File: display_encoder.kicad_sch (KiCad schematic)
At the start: 9 parts

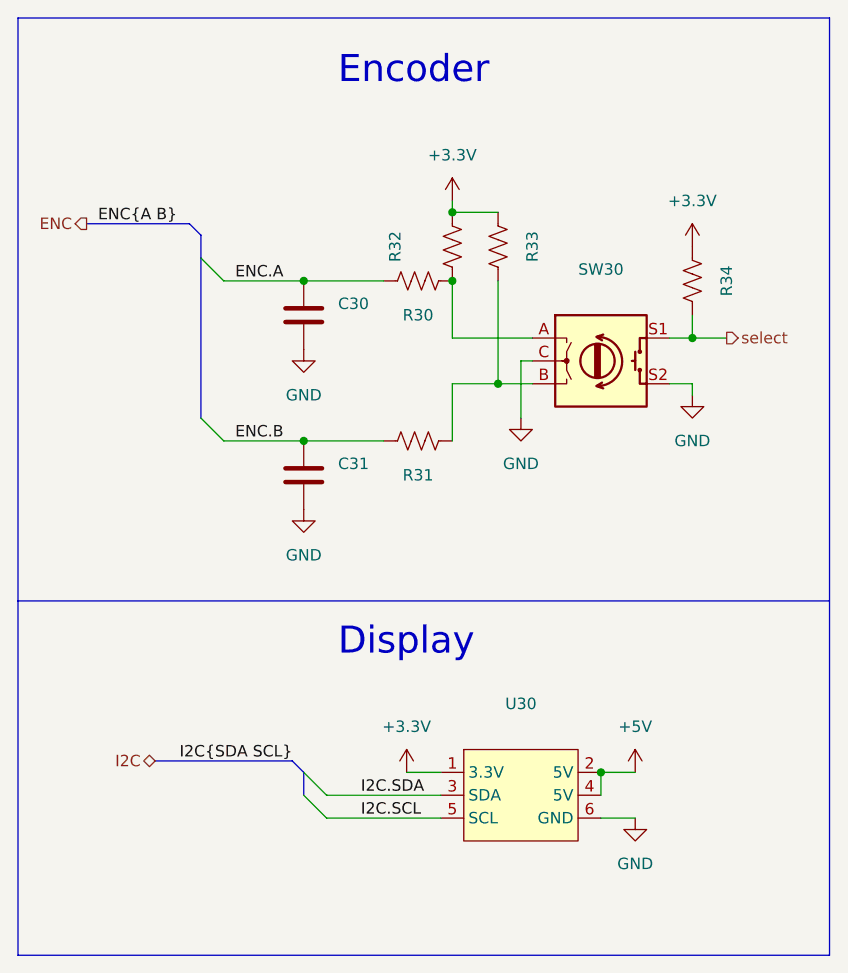
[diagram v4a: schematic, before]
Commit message: Add heatsink, among other things
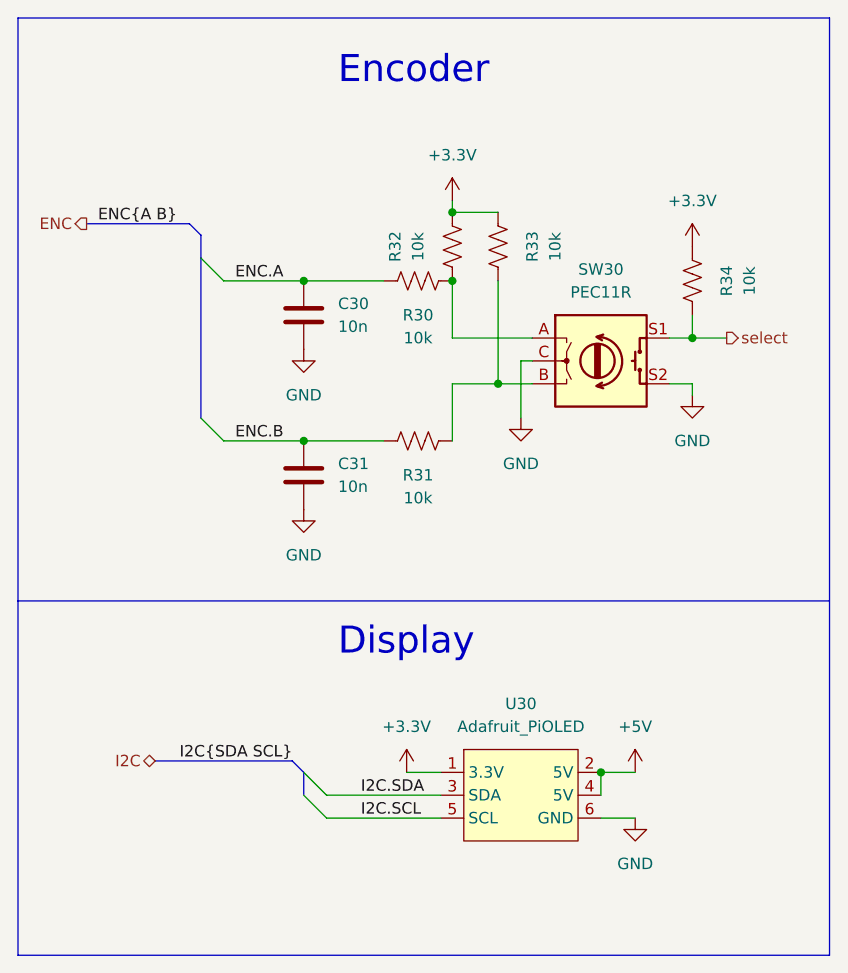
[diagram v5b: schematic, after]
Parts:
- C30, C31: value (none) -> 10n; footprint (none) -> Capacitor_SMD:C_0805_2012Metric
- R30, R31, R32, R33, R34: value (none) -> 10k; footprint (none) -> Resistor_SMD:R_0805_2012Metric
- SW30: value (none) -> PEC11R; footprint (none) -> Rotary_Encoder:RotaryEncoder_Alps_EC12E-Switch_Vertical_H20mm
- U30: value (none) -> Adafruit_PiOLED; footprint (none) -> 0_Display:PiOLED
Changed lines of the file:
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@@
     (in_bom yes) (on_board yes)
     (property "Reference" "R30" (id 0) (at 149.86 73.66 90))
-    (property "Value" "" (id 1) (at 149.86 76.2 90))
-    (property "Footprint" "" (id 2) (at 150.114 68.834 90)
+    (property "Value" "10k" (id 1) (at 149.86 76.2 90))
+    (property "Footprint" "Resistor_SMD:R_0805_2012Metric" (id 2) (at 150.114 68.834 90)
       (effects (font (size 1.27 1.27)) hide)
     )
@@
     (in_bom yes) (on_board yes) (fields_autoplaced)
     (property "Reference" "U30" (id 0) (at 161.29 116.84 0))
-    (property "Value" "" (id 1) (at 161.29 119.38 0))
-    (property "Footprint" "" (id 2) (at 162.56 121.92 0)
+    (property "Value" "Adafruit_PiOLED" (id 1) (at 161.29 119.38 0))
+    (property "Footprint" "0_Display:PiOLED" (id 2) (at 162.56 121.92 0)
       (effects (font (size 1.27 1.27)) hide)
     )
@@
       (effects (font (size 1.27 1.27)) (justify right))
     )
-    (property "Value" "" (id 1) (at 140.97 74.9299 0)
-      (effects (font (size 1.27 1.27)) (justify right))
-    )
-    (property "Footprint" "" (id 2) (at 136.1948 69.85 0)
+    (property "Value" "10n" (id 1) (at 140.97 74.9299 0)
+      (effects (font (size 1.27 1.27)) (justify right))
+    )
+    (property "Footprint" "Capacitor_SMD:C_0805_2012Metric" (id 2) (at 136.1948 69.85 0)
       (effects (font (size 1.27 1.27)) hide)
     )
@@
     (in_bom yes) (on_board yes)
     (property "Reference" "SW30" (id 0) (at 170.18 68.58 0))
-    (property "Value" "" (id 1) (at 170.18 71.12 0))
-    (property "Footprint" "" (id 2) (at 166.37 74.676 0)
+    (property "Value" "PEC11R" (id 1) (at 170.18 71.12 0))
+    (property "Footprint" "Rotary_Encoder:RotaryEncoder_Alps_EC12E-Switch_Vertical_H20mm" (id 2) (at 166.37 74.676 0)
       (effects (font (size 1.27 1.27)) hide)
     )
@@
       (effects (font (size 1.27 1.27)) (justify right))
     )
-    (property "Value" "" (id 1) (at 140.97 92.7099 0)
-      (effects (font (size 1.27 1.27)) (justify right))
-    )
-    (property "Footprint" "" (id 2) (at 136.1948 87.63 0)
+    (property "Value" "10n" (id 1) (at 140.97 92.7099 0)
+      (effects (font (size 1.27 1.27)) (justify right))
+    )
+    (property "Footprint" "Capacitor_SMD:C_0805_2012Metric" (id 2) (at 136.1948 87.63 0)
       (effects (font (size 1.27 1.27)) hide)
     )
@@
     (in_bom yes) (on_board yes)
     (property "Reference" "R32" (id 0) (at 147.32 66.04 90))
-    (property "Value" "" (id 1) (at 149.86 66.04 90))
-    (property "Footprint" "" (id 2) (at 154.686 66.294 90)
+    (property "Value" "10k" (id 1) (at 149.86 66.04 90))
+    (property "Footprint" "Resistor_SMD:R_0805_2012Metric" (id 2) (at 154.686 66.294 90)
       (effects (font (size 1.27 1.27)) hide)
     )
@@
     (in_bom yes) (on_board yes)
     (property "Reference" "R34" (id 0) (at 184.15 69.85 90))
-    (property "Value" "" (id 1) (at 186.69 69.85 90))
-    (property "Footprint" "" (id 2) (at 179.324 69.596 90)
+    (property "Value" "10k" (id 1) (at 186.69 69.85 90))
+    (property "Footprint" "Resistor_SMD:R_0805_2012Metric" (id 2) (at 179.324 69.596 90)
       (effects (font (size 1.27 1.27)) hide)
     )
@@
     (in_bom yes) (on_board yes)
     (property "Reference" "R31" (id 0) (at 149.86 91.44 90))
-    (property "Value" "" (id 1) (at 149.86 93.98 90))
-    (property "Footprint" "" (id 2) (at 150.114 86.614 90)
+    (property "Value" "10k" (id 1) (at 149.86 93.98 90))
+    (property "Footprint" "Resistor_SMD:R_0805_2012Metric" (id 2) (at 150.114 86.614 90)
       (effects (font (size 1.27 1.27)) hide)
     )
@@
     (in_bom yes) (on_board yes)
     (property "Reference" "R33" (id 0) (at 162.56 66.04 90))
-    (property "Value" "" (id 1) (at 165.1 66.04 90))
-    (property "Footprint" "" (id 2) (at 157.734 65.786 90)
-      (effects (font (size 1.27 1.27)) hide)
-    )
+    (property "Value" "10k" (id 1) (at 165.1 66.04 90))
+    (property "Footprint" "Resistor_SMD:R_0805_2012Metric" (id 2) (at 157.734 65.786 90)
+      (effects (font (size 1.27 1.27)) hide)
+    )

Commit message: WIP routing
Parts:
- C601: renamed from C30; value 10n -> (none); footprint Capacitor_SMD:C_0805_2012Metric -> (none)
- C602: renamed from C31; value 10n -> (none); footprint Capacitor_SMD:C_0805_2012Metric -> (none)
- R601: renamed from R30; value 10k -> (none); footprint Resistor_SMD:R_0805_2012Metric -> (none)
- R602: renamed from R31; value 10k -> (none); footprint Resistor_SMD:R_0805_2012Metric -> (none)
- R603: renamed from R32; value 10k -> (none); footprint Resistor_SMD:R_0805_2012Metric -> (none)
- R604: renamed from R33; value 10k -> (none); footprint Resistor_SMD:R_0805_2012Metric -> (none)
- R605: renamed from R34; value 10k -> (none); footprint Resistor_SMD:R_0805_2012Metric -> (none)
- SW601: renamed from SW30; value PEC11R -> (none); footprint Rotary_Encoder:RotaryEncoder_Alps_EC12E-Switch_Vertical_H20mm -> (none)
- U601: renamed from U30; value Adafruit_PiOLED -> (none); footprint 0_Display:PiOLED -> (none)
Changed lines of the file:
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@@
   (symbol (lib_id "power:GND") (at 137.16 77.47 0) (unit 1)
     (in_bom yes) (on_board yes) (fields_autoplaced)
-    (property "Reference" "#PWR0118" (id 0) (at 137.16 83.82 0)
+    (property "Reference" "#PWR0601" (id 0) (at 137.16 83.82 0)
       (effects (font (size 1.27 1.27)) hide)
     )
@@
   (symbol (lib_id "power:+3.3V") (at 180.34 66.04 0) (unit 1)
     (in_bom yes) (on_board yes) (fields_autoplaced)
-    (property "Reference" "#PWR0120" (id 0) (at 180.34 69.85 0)
+    (property "Reference" "#PWR0608" (id 0) (at 180.34 69.85 0)
       (effects (font (size 1.27 1.27)) hide)
     )
@@
   (symbol (lib_id "Device:R_US") (at 149.86 69.85 90) (unit 1)
     (in_bom yes) (on_board yes)
-    (property "Reference" "R30" (id 0) (at 149.86 73.66 90))
-    (property "Value" "10k" (id 1) (at 149.86 76.2 90))
-    (property "Footprint" "Resistor_SMD:R_0805_2012Metric" (id 2) (at 150.114 68.834 90)
+    (property "Reference" "R601" (id 0) (at 149.86 73.66 90))
+    (property "Value" "" (id 1) (at 149.86 76.2 90))
+    (property "Footprint" "" (id 2) (at 150.114 68.834 90)
       (effects (font (size 1.27 1.27)) hide)
     )
@@
   (symbol (lib_id "0_Display_Graphic:Adafruit_PiOLED") (at 161.29 127 0) (unit 1)
     (in_bom yes) (on_board yes) (fields_autoplaced)
-    (property "Reference" "U30" (id 0) (at 161.29 116.84 0))
-    (property "Value" "Adafruit_PiOLED" (id 1) (at 161.29 119.38 0))
-    (property "Footprint" "0_Display:PiOLED" (id 2) (at 162.56 121.92 0)
+    (property "Reference" "U601" (id 0) (at 161.29 116.84 0))
+    (property "Value" "" (id 1) (at 161.29 119.38 0))
+    (property "Footprint" "" (id 2) (at 162.56 121.92 0)
       (effects (font (size 1.27 1.27)) hide)
     )
@@
   (symbol (lib_id "power:GND") (at 173.99 129.54 0) (unit 1)
     (in_bom yes) (on_board yes) (fields_autoplaced)
-    (property "Reference" "#PWR0106" (id 0) (at 173.99 135.89 0)
+    (property "Reference" "#PWR0607" (id 0) (at 173.99 135.89 0)
       (effects (font (size 1.27 1.27)) hide)
     )
@@
   (symbol (lib_id "power:GND") (at 180.34 82.55 0) (unit 1)
     (in_bom yes) (on_board yes) (fields_autoplaced)
-    (property "Reference" "#PWR0119" (id 0) (at 180.34 88.9 0)
+    (property "Reference" "#PWR0609" (id 0) (at 180.34 88.9 0)
       (effects (font (size 1.27 1.27)) hide)
     )
@@
   (symbol (lib_id "power:GND") (at 161.29 85.09 0) (unit 1)
     (in_bom yes) (on_board yes) (fields_autoplaced)
-    (property "Reference" "#PWR0116" (id 0) (at 161.29 91.44 0)
+    (property "Reference" "#PWR0605" (id 0) (at 161.29 91.44 0)
       (effects (font (size 1.27 1.27)) hide)
     )
@@
   (symbol (lib_id "power:GND") (at 137.16 95.25 0) (unit 1)
     (in_bom yes) (on_board yes) (fields_autoplaced)
-    (property "Reference" "#PWR0117" (id 0) (at 137.16 101.6 0)
+    (property "Reference" "#PWR0602" (id 0) (at 137.16 101.6 0)
       (effects (font (size 1.27 1.27)) hide)
     )
@@
   (symbol (lib_id "Device:C") (at 137.16 73.66 180) (unit 1)
     (in_bom yes) (on_board yes) (fields_autoplaced)
-    (property "Reference" "C30" (id 0) (at 140.97 72.3899 0)
-      (effects (font (size 1.27 1.27)) (justify right))
-    )
-    (property "Value" "10n" (id 1) (at 140.97 74.9299 0)
-      (effects (font (size 1.27 1.27)) (justify right))
-    )
-    (property "Footprint" "Capacitor_SMD:C_0805_2012Metric" (id 2) (at 136.1948 69.85 0)
+    (property "Reference" "C601" (id 0) (at 140.97 72.3899 0)
+      (effects (font (size 1.27 1.27)) (justify right))
+    )
+    (property "Value" "" (id 1) (at 140.97 74.9299 0)
+      (effects (font (size 1.27 1.27)) (justify right))
+    )
+    (property "Footprint" "" (id 2) (at 136.1948 69.85 0)
       (effects (font (size 1.27 1.27)) hide)
     )
@@
   (symbol (lib_id "Device:RotaryEncoder_Switch") (at 170.18 78.74 0) (unit 1)
     (in_bom yes) (on_board yes)
-    (property "Reference" "SW30" (id 0) (at 170.18 68.58 0))
-    (property "Value" "PEC11R" (id 1) (at 170.18 71.12 0))
-    (property "Footprint" "Rotary_Encoder:RotaryEncoder_Alps_EC12E-Switch_Vertical_H20mm" (id 2) (at 166.37 74.676 0)
+    (property "Reference" "SW601" (id 0) (at 170.18 68.58 0))
+    (property "Value" "" (id 1) (at 170.18 71.12 0))
+    (property "Footprint" "" (id 2) (at 166.37 74.676 0)
       (effects (font (size 1.27 1.27)) hide)
     )
@@
   (symbol (lib_id "Device:C") (at 137.16 91.44 180) (unit 1)
     (in_bom yes) (on_board yes) (fields_autoplaced)
-    (property "Reference" "C31" (id 0) (at 140.97 90.1699 0)
-      (effects (font (size 1.27 1.27)) (justify right))
-    )
-    (property "Value" "10n" (id 1) (at 140.97 92.7099 0)
-      (effects (font (size 1.27 1.27)) (justify right))
-    )
-    (property "Footprint" "Capacitor_SMD:C_0805_2012Metric" (id 2) (at 136.1948 87.63 0)
+    (property "Reference" "C602" (id 0) (at 140.97 90.1699 0)
+      (effects (font (size 1.27 1.27)) (justify right))
+    )
+    (property "Value" "" (id 1) (at 140.97 92.7099 0)
+      (effects (font (size 1.27 1.27)) (justify right))
+    )
+    (property "Footprint" "" (id 2) (at 136.1948 87.63 0)
       (effects (font (size 1.27 1.27)) hide)
     )
@@
   (symbol (lib_id "power:+3.3V") (at 148.59 124.46 0) (unit 1)
     (in_bom yes) (on_board yes) (fields_autoplaced)
-    (property "Reference" "#PWR0104" (id 0) (at 148.59 128.27 0)
+    (property "Reference" "#PWR0603" (id 0) (at 148.59 128.27 0)
       (effects (font (size 1.27 1.27)) hide)
     )
@@
   (symbol (lib_id "Device:R_US") (at 153.67 66.04 0) (unit 1)
     (in_bom yes) (on_board yes)
-    (property "Reference" "R32" (id 0) (at 147.32 66.04 90))
-    (property "Value" "10k" (id 1) (at 149.86 66.04 90))
-    (property "Footprint" "Resistor_SMD:R_0805_2012Metric" (id 2) (at 154.686 66.294 90)
+    (property "Reference" "R603" (id 0) (at 147.32 66.04 90))
+    (property "Value" "" (id 1) (at 149.86 66.04 90))
+    (property "Footprint" "" (id 2) (at 154.686 66.294 90)
       (effects (font (size 1.27 1.27)) hide)
     )
@@
   (symbol (lib_id "Device:R_US") (at 180.34 69.85 180) (unit 1)
     (in_bom yes) (on_board yes)
-    (property "Reference" "R34" (id 0) (at 184.15 69.85 90))
-    (property "Value" "10k" (id 1) (at 186.69 69.85 90))
-    (property "Footprint" "Resistor_SMD:R_0805_2012Metric" (id 2) (at 179.324 69.596 90)
+    (property "Reference" "R605" (id 0) (at 184.15 69.85 90))
+    (property "Value" "" (id 1) (at 186.69 69.85 90))
+    (property "Footprint" "" (id 2) (at 179.324 69.596 90)
       (effects (font (size 1.27 1.27)) hide)
     )
@@
   (symbol (lib_id "power:+5V") (at 173.99 124.46 0) (unit 1)
     (in_bom yes) (on_board yes) (fields_autoplaced)
-    (property "Reference" "#PWR0105" (id 0) (at 173.99 128.27 0)
+    (property "Reference" "#PWR0606" (id 0) (at 173.99 128.27 0)
       (effects (font (size 1.27 1.27)) hide)
     )
@@
   (symbol (lib_id "Device:R_US") (at 149.86 87.63 90) (unit 1)
     (in_bom yes) (on_board yes)
-    (property "Reference" "R31" (id 0) (at 149.86 91.44 90))
-    (property "Value" "10k" (id 1) (at 149.86 93.98 90))
-    (property "Footprint" "Resistor_SMD:R_0805_2012Metric" (id 2) (at 150.114 86.614 90)
+    (property "Reference" "R602" (id 0) (at 149.86 91.44 90))
+    (property "Value" "" (id 1) (at 149.86 93.98 90))
+    (property "Footprint" "" (id 2) (at 150.114 86.614 90)
       (effects (font (size 1.27 1.27)) hide)
     )
@@
   (symbol (lib_id "power:+3.3V") (at 153.67 60.96 0) (unit 1)
     (in_bom yes) (on_board yes) (fields_autoplaced)
-    (property "Reference" "#PWR0115" (id 0) (at 153.67 64.77 0)
+    (property "Reference" "#PWR0604" (id 0) (at 153.67 64.77 0)
       (effects (font (size 1.27 1.27)) hide)
     )
@@
   (symbol (lib_id "Device:R_US") (at 158.75 66.04 180) (unit 1)
     (in_bom yes) (on_board yes)
-    (property "Reference" "R33" (id 0) (at 162.56 66.04 90))
-    (property "Value" "10k" (id 1) (at 165.1 66.04 90))
-    (property "Footprint" "Resistor_SMD:R_0805_2012Metric" (id 2) (at 157.734 65.786 90)
-      (effects (font (size 1.27 1.27)) hide)
-    )
+    (property "Reference" "R604" (id 0) (at 162.56 66.04 90))
+    (property "Value" "" (id 1) (at 165.1 66.04 90))
+    (property "Footprint" "" (id 2) (at 157.734 65.786 90)
+      (effects (font (size 1.27 1.27)) hide)
+    )
